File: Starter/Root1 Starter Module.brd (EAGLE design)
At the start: 25.4 x 25.4 mm, 2 parts

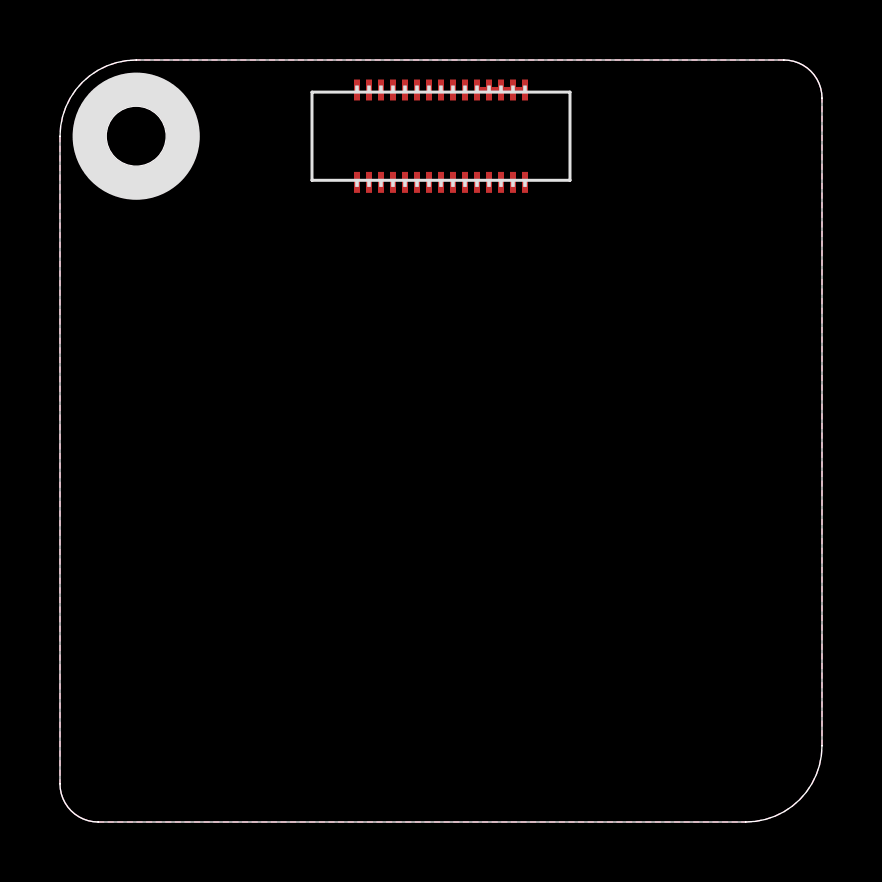
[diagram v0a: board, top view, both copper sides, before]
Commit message: Root1 Starter Module:  - Updated connectors  - Dual sided  - Dual #2 screw holes
Signed-off-by: Cruz Monrreal II <Cruz.Monrreal@gmail.com>
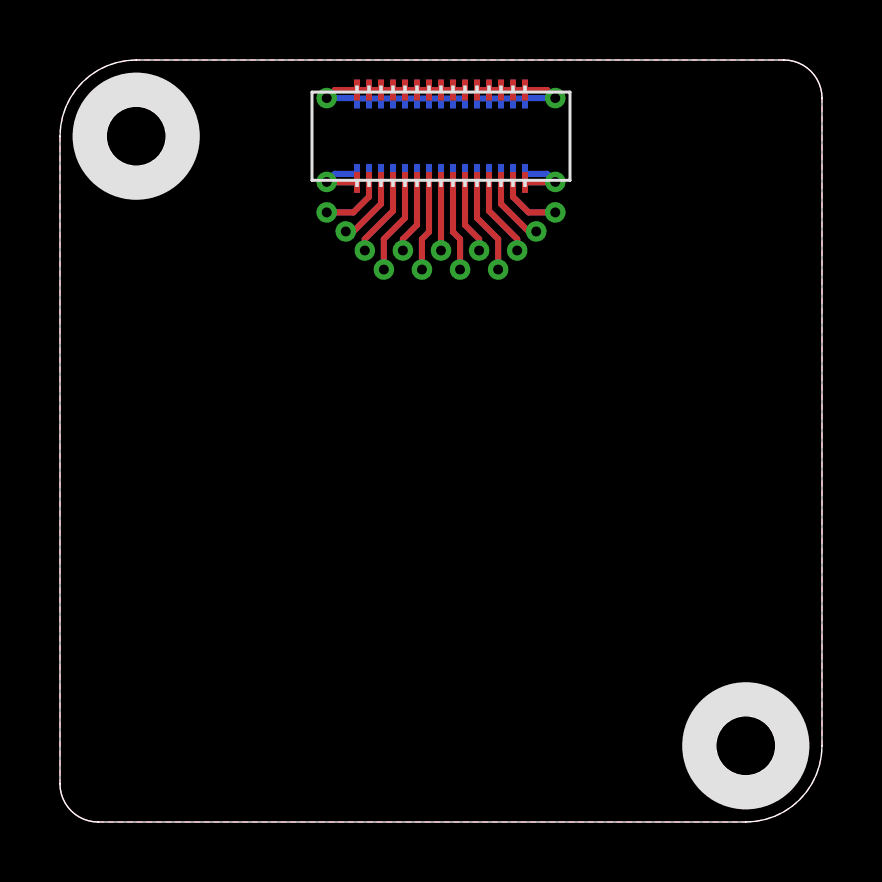
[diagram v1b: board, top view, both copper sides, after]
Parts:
- removed U$2: ROOT1, thinkmaketest:ROOT1.TOP
- added U$3: HOLE.2MM, .screw_holes:2MM
- added U$8: ROOT1.BOTH, thinkmaketest:ROOT1.BOTH
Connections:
- net 3.3V: now also U$8.3.3V@1, U$8.3.3V@10, U$8.3.3V@2, U$8.3.3V@3, U$8.3.3V@4, U$8.3.3V@5, U$8.3.3V@6, U$8.3.3V@7, U$8.3.3V@8, U$8.3.3V@9, U$8.3.3V@VIA; no longer U$2.16, U$2.17, U$2.18, U$2.19, U$2.20
- net GND: now also U$8.GND@1, U$8.GND@10, U$8.GND@11, U$8.GND@12, U$8.GND@13, U$8.GND@14, U$8.GND@15, U$8.GND@16, U$8.GND@17, U$8.GND@18, U$8.GND@19, U$8.GND@2, U$8.GND@20, U$8.GND@3, U$8.GND@4, U$8.GND@5, U$8.GND@6, U$8.GND@7, U$8.GND@8, U$8.GND@9, U$8.GND@VIA; no longer U$2.21, U$2.22, U$2.23, U$2.24, U$2.25, U$2.26, U$2.27, U$2.28, U$2.29, U$2.30
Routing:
- net 3.3V: track 1.60 -> 0.00 mm

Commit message: Updated Starter Module w/ standard location and new connector spacing
Signed-off-by: Cruz Monrreal II <Cruz.Monrreal@gmail.com>
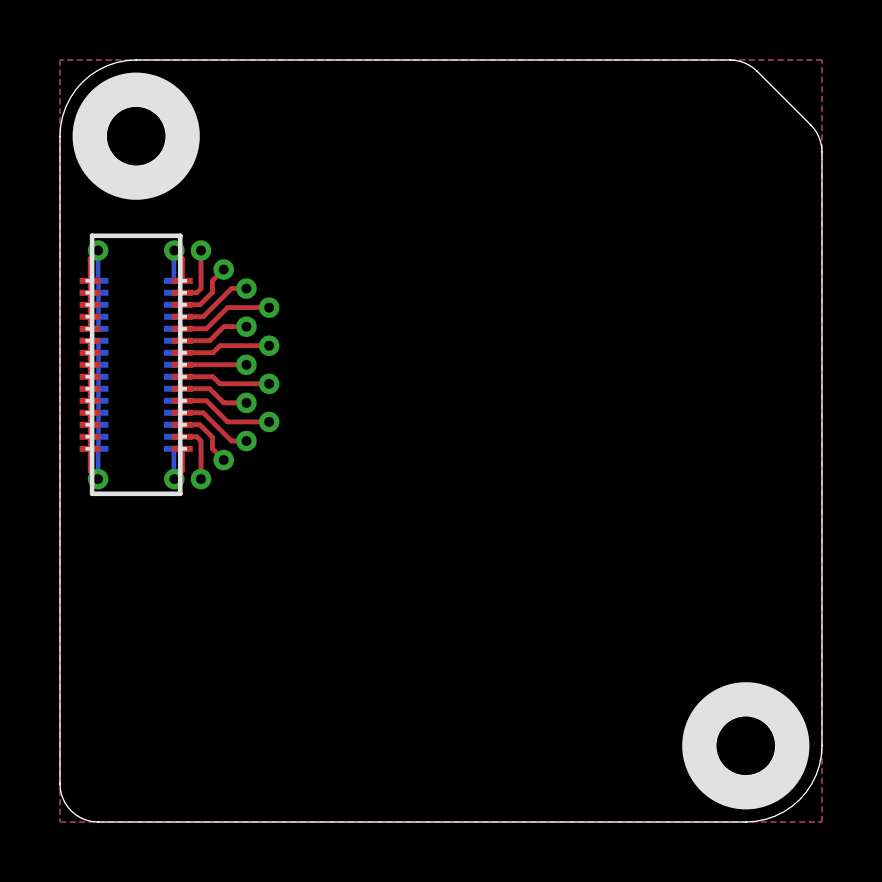
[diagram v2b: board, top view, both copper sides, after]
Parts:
- turned U$3 to 90 degrees
- turned U$4 to 90 degrees
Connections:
- new net N$1: U$8.ADC0, U$8.ADC0@1, U$8.ADC0@VIA
- new net N$10: U$8.03, U$8.03@1, U$8.03@VIA
- new net N$11: U$8.04, U$8.04@1, U$8.04@VIA
- new net N$12: U$8.05, U$8.05@1, U$8.05@VIA
- new net N$13: U$8.06, U$8.06@1, U$8.06@VIA
- new net N$14: U$8.07, U$8.07@1, U$8.07@VIA
- new net N$15: U$8.WAKE, U$8.WAKE@1, U$8.WAKE@VIA
- new net N$2: U$8.ADC1, U$8.ADC1@1, U$8.ADC1@VIA
- new net N$3: U$8.SDA, U$8.SDA@1, U$8.SDA@VIA
- new net N$4: U$8.SCL, U$8.SCL@1, U$8.SCL@VIA
- new net N$5: U$8.MOSI, U$8.MOSI@1, U$8.MOSI@VIA
- new net N$6: U$8.MISO, U$8.MISO@1, U$8.MISO@VIA
- new net N$7: U$8.SCLK, U$8.SCLK@1, U$8.SCLK@VIA
- new net N$8: U$8.01, U$8.01@1, U$8.01@VIA
- new net N$9: U$8.02, U$8.02@1, U$8.02@VIA
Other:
- outline, holes or cut-outs redrawn
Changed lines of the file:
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@@
 <?xml version="1.0" encoding="utf-8"?>
 <!DOCTYPE eagle SYSTEM "eagle.dtd">
-<eagle version="6.2">
+<eagle version="6.1">
 <drawing>
 <settings>
@@
 <board>
 <plain>
-<wire x1="24.13" y1="25.4" x2="2.54" y2="25.4" width="0" layer="20"/>
-<wire x1="2.54" y1="25.4" x2="0" y2="22.86" width="0" layer="20" curve="90"/>
 <wire x1="0" y1="22.86" x2="0" y2="1.27" width="0" layer="20"/>
 <wire x1="0" y1="1.27" x2="1.27" y2="0" width="0" layer="20" curve="90"/>
 <wire x1="1.27" y1="0" x2="22.86" y2="0" width="0" layer="20"/>
 <wire x1="22.86" y1="0" x2="25.4" y2="2.54" width="0" layer="20" curve="90"/>
-<wire x1="25.4" y1="2.54" x2="25.4" y2="24.13" width="0" layer="20"/>
-<wire x1="25.4" y1="24.13" x2="24.13" y2="25.4" width="0" layer="20" curve="90"/>
+<wire x1="25.4" y1="2.54" x2="25.4" y2="22.33395" width="0" layer="20"/>
+<wire x1="25.4" y1="22.33395" x2="25.028025" y2="23.231975" width="0" layer="20" curve="45"/>
+<wire x1="25.028025" y1="23.231975" x2="23.231975" y2="25.028025" width="0" layer="20"/>
+<wire x1="23.231975" y1="25.028025" x2="22.33395" y2="25.4" width="0" layer="20" curve="45"/>
+<wire x1="22.33395" y1="25.4" x2="2.54" y2="25.4" width="0" layer="20"/>
+<wire x1="2.54" y1="25.4" x2="0" y2="22.86" width="0" layer="20" curve="90"/>
 </plain>
 <attributes>
@@
 <param name="checkFont" value="1"/>
 <param name="checkRestrict" value="1"/>
-<param name="useDiameter" value="15"/>
+<param name="useDiameter" value="13"/>
 <param name="maxErrors" value="50"/>
 </designrules>
@@
 </autorouter>
 <elements>
-<element name="U$4" library=".screw_holes" package="2MM" value="HOLE.2MM" x="2.54" y="22.86"/>
-<element name="U$3" library=".screw_holes" package="2MM" value="HOLE.2MM" x="22.86" y="2.54"/>
+<element name="U$4" library=".screw_holes" package="2MM" value="HOLE.2MM" x="2.54" y="22.86" rot="R90"/>
+<element name="U$3" library=".screw_holes" package="2MM" value="HOLE.2MM" x="22.86" y="2.54" rot="R90"/>
 <element name="U$8" library="thinkmaketest" package="ROOT1.BOTH" value="ROOT1.BOTH" x="0" y="0"/>
 </elements>
@@
 <signal name="GND">
 <polygon width="0.2032" layer="16">
-<vertex x="24.13" y="25.4"/>
-<vertex x="2.54" y="25.4" curve="90"/>
-<vertex x="0" y="22.86"/>
-<vertex x="0" y="1.27" curve="90"/>
-<vertex x="1.27" y="0"/>
-<vertex x="22.86" y="0" curve="90"/>
-<vertex x="25.4" y="2.54"/>
-<vertex x="25.4" y="24.13" curve="90"/>
+<vertex x="0" y="0"/>
+<vertex x="25.4" y="0"/>
+<vertex x="25.4" y="25.4"/>
+<vertex x="0" y="25.4"/>
 </polygon>
 <polygon width="0.2032" layer="1">
-<vertex x="24.13" y="25.4"/>
-<vertex x="2.54" y="25.4" curve="90"/>
-<vertex x="0" y="22.86"/>
-<vertex x="0" y="1.27" curve="90"/>
-<vertex x="1.27" y="0"/>
-<vertex x="22.86" y="0" curve="90"/>
-<vertex x="25.4" y="2.54"/>
-<vertex x="25.4" y="24.13" curve="90"/>
+<vertex x="0" y="0"/>
+<vertex x="25.4" y="0"/>
+<vertex x="25.4" y="25.4"/>
+<vertex x="0" y="25.4"/>
 </polygon>
 <contactref element="U$8" pad="GND@17"/>
@@
 <contactref element="U$8" pad="3.3V@VIA"/>
 </signal>
+<signal name="N$1">
+<contactref element="U$8" pad="ADC0@1"/>
+<contactref element="U$8" pad="ADC0"/>
+<contactref element="U$8" pad="ADC0@VIA"/>
+</signal>
+<signal name="N$2">
+<contactref element="U$8" pad="ADC1"/>
+<contactref element="U$8" pad="ADC1@1"/>
+<contactref element="U$8" pad="ADC1@VIA"/>
+</signal>
+<signal name="N$3">
+<contactref element="U$8" pad="SDA"/>
+<contactref element="U$8" pad="SDA@1"/>
+<contactref element="U$8" pad="SDA@VIA"/>
+</signal>
+<signal name="N$4">
+<contactref element="U$8" pad="SCL"/>
+<contactref element="U$8" pad="SCL@1"/>
+<contactref element="U$8" pad="SCL@VIA"/>
+</signal>
+<signal name="N$5">
+<contactref element="U$8" pad="MOSI@VIA"/>
+<contactref element="U$8" pad="MOSI"/>
+<contactref element="U$8" pad="MOSI@1"/>
+</signal>
+<signal name="N$6">
+<contactref element="U$8" pad="MISO"/>
+<contactref element="U$8" pad="MISO@VIA"/>
+<contactref element="U$8" pad="MISO@1"/>
+</signal>
+<signal name="N$7">
+<contactref element="U$8" pad="SCLK@1"/>
+<contactref element="U$8" pad="SCLK"/>
+<contactref element="U$8" pad="SCLK@VIA"/>
+</signal>
+<signal name="N$8">
+<contactref element="U$8" pad="01@VIA"/>
+<contactref element="U$8" pad="01@1"/>
+<contactref element="U$8" pad="01"/>
+</signal>
+<signal name="N$9">
+<contactref element="U$8" pad="02@VIA"/>
+<contactref element="U$8" pad="02@1"/>
+<contactref element="U$8" pad="02"/>
+</signal>
+<signal name="N$10">
+<contactref element="U$8" pad="03@1"/>
+<contactref element="U$8" pad="03@VIA"/>
+<contactref element="U$8" pad="03"/>
+</signal>
+<signal name="N$11">
+<contactref element="U$8" pad="04@VIA"/>
+<contactref element="U$8" pad="04@1"/>
+<contactref element="U$8" pad="04"/>
+</signal>
+<signal name="N$12">
+<contactref element="U$8" pad="05"/>
+<contactref element="U$8" pad="05@VIA"/>
+<contactref element="U$8" pad="05@1"/>
+</signal>
+<signal name="N$13">
+<contactref element="U$8" pad="06"/>
+<contactref element="U$8" pad="06@VIA"/>
+<contactref element="U$8" pad="06@1"/>
+</signal>
+<signal name="N$14">
+<contactref element="U$8" pad="07@VIA"/>
+<contactref element="U$8" pad="07@1"/>
+<contactref element="U$8" pad="07"/>
+</signal>
+<signal name="N$15">
+<contactref element="U$8" pad="WAKE@VIA"/>
+<contactref element="U$8" pad="WAKE@1"/>
+<contactref element="U$8" pad="WAKE"/>
+</signal>
 </signals>
